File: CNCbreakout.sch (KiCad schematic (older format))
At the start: 18 parts, among them P101 X1, P102 X2, P103 Y, P104 Z, P105 GND, P106 +24V, P107 VFD_Stop, P108 VFD_FwdRev, P109 VFD_Aux, P110 Z_STOP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

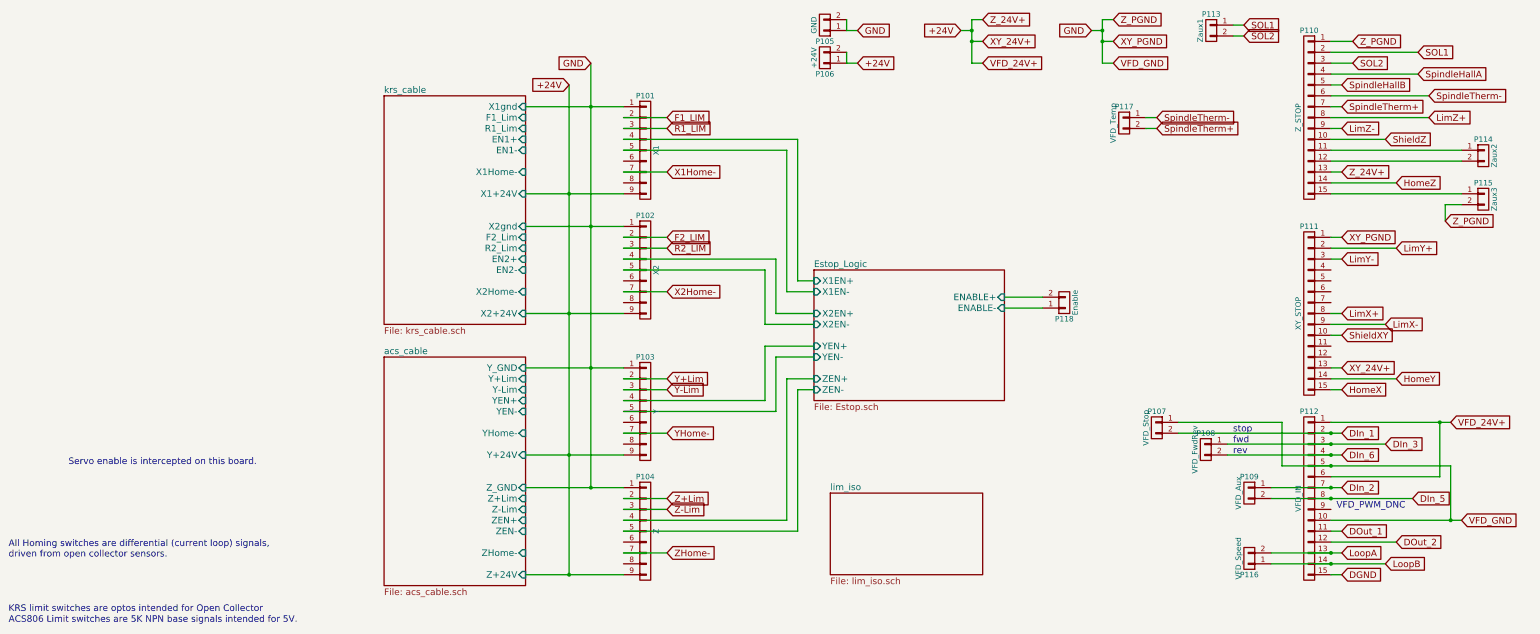
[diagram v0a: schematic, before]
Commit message: checked limits and homes, removed enable, adjusted routing
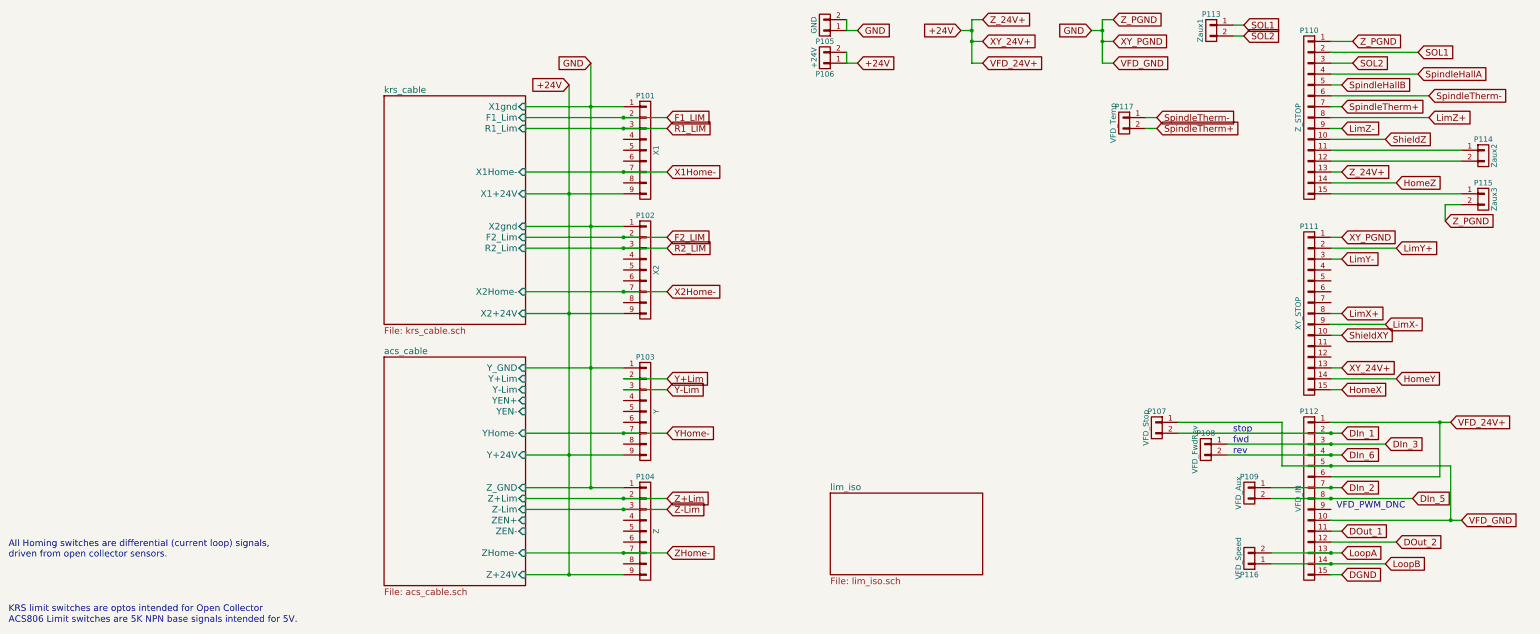
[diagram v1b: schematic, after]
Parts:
- removed P118: Enable, Connect:bornier2, symbol CONN_01X02
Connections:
- net Estop_Logic/X1EN+: no longer names the net of P101.4 (P4)
- net Estop_Logic/X1EN-: no longer names the net of P101.5 (P5)
- net Estop_Logic/X2EN+: no longer names the net of P102.4 (P4)
- net Estop_Logic/X2EN-: no longer names the net of P102.5 (P5)
- net Estop_Logic/YEN+: no longer names the net of P103.4 (P4)
- net Estop_Logic/YEN-: no longer names the net of P103.5 (P5)
- net Estop_Logic/ZEN+: no longer names the net of P104.4 (P4)
- net Estop_Logic/ZEN-: no longer names the net of P104.5 (P5)
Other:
- note removed: "Servo enable is intercepted on this board."
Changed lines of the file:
@@
 $Descr A4 11693 8268
 encoding utf-8
-Sheet 1 5
+Sheet 1 4
 Title ""
 Date ""
@@
 F3 "F1_Lim" I R 2100 1700 60
 F4 "R1_Lim" I R 2100 1800 60
-F5 "EN1+" I R 2100 1900 60
-F6 "EN1-" I R 2100 2000 60
-F7 "X1Home-" I R 2100 2200 60
-F8 "X1+24V" I R 2100 2400 60
-F9 "X2gnd" I R 2100 2700 60
-F10 "F2_Lim" I R 2100 2800 60
-F11 "R2_Lim" I R 2100 2900 60
-F12 "EN2+" I R 2100 3000 60
-F13 "EN2-" I R 2100 3100 60
-F14 "X2Home-" I R 2100 3300 60
-F15 "X2+24V" I R 2100 3500 60
+F5 "X1Home-" I R 2100 2200 60
+F6 "X1+24V" I R 2100 2400 60
+F7 "X2gnd" I R 2100 2700 60
+F8 "F2_Lim" I R 2100 2800 60
+F9 "R2_Lim" I R 2100 2900 60
+F10 "X2Home-" I R 2100 3300 60
+F11 "X2+24V" I R 2100 3500 60
 $EndSheet
-Text Notes -2100 4900 0    60   ~ 0
-Servo enable is intercepted on this board.
 Text GLabel 3400 2900 2    60   Input ~ 0
 R2_LIM
@@
 Text GLabel 7500 1200 2    60   Input ~ 0
 VFD_GND
-$Sheet
-S 4750 3100 1750 1200
-U 5792E5FC
-F0 "Estop_Logic" 60
-F1 "Estop.sch" 60
-F2 "ZEN+" I L 4750 4100 60
-F3 "ZEN-" I L 4750 4200 60
-F4 "YEN+" I L 4750 3800 60
-F5 "YEN-" I L 4750 3900 60
-F6 "X1EN+" I L 4750 3200 60
-F7 "X1EN-" I L 4750 3300 60
-F8 "X2EN+" I L 4750 3500 60
-F9 "X2EN-" I L 4750 3600 60
-F10 "ENABLE+" I R 6500 3350 60
-F11 "ENABLE-" I R 6500 3450 60
-$EndSheet
 Wire Wire Line
 	9700 1000 9500 1000
@@
 Connection ~ 7400 1000
 Wire Wire Line
-	3400 1700 3000 1700
-Wire Wire Line
-	3000 1800 3400 1800
-Wire Wire Line
-	3000 2200 3400 2200
-Wire Wire Line
-	3400 2800 3000 2800
-Wire Wire Line
-	3000 3300 3400 3300
-Wire Wire Line
-	3400 2900 3000 2900
+	2100 1700 3400 1700
+Wire Wire Line
+	2100 1800 3400 1800
+Wire Wire Line
+	2100 2200 3400 2200
+Wire Wire Line
+	2100 2800 3400 2800
+Wire Wire Line
+	2100 3300 3400 3300
+Wire Wire Line
+	2100 2900 3400 2900
 Wire Wire Line
 	3400 4100 3000 4100
@@
 	3000 4200 3400 4200
 Wire Wire Line
-	3000 4600 3400 4600
+	2100 4600 3400 4600
 Connection ~ 2700 5100
 Wire Wire Line
-	3000 5200 3400 5200
-Wire Wire Line
-	3400 5300 3000 5300
-Wire Wire Line
-	3400 5700 3000 5700
+	2100 5200 3400 5200
+Wire Wire Line
+	2100 5300 3400 5300
+Wire Wire Line
+	2100 5700 3400 5700
 Connection ~ 2500 5900
 $Comp
@@
 	-1   0    0    -1
 $EndComp
-Wire Wire Line
-	4750 3200 4600 3200
-Wire Wire Line
-	4600 3200 4600 1900
-Wire Wire Line
-	4600 1900 3000 1900
-Wire Wire Line
-	3000 2000 4500 2000
-Wire Wire Line
-	4500 2000 4500 3300
-Wire Wire Line
-	4500 3300 4750 3300
-Wire Wire Line
-	4750 3500 4400 3500
-Wire Wire Line
-	4400 3500 4400 3000
-Wire Wire Line
-	4400 3000 3000 3000
-Wire Wire Line
-	3000 3100 4300 3100
-Wire Wire Line
-	4300 3100 4300 3600
-Wire Wire Line
-	4300 3600 4750 3600
-Wire Wire Line
-	4750 3800 4300 3800
-Wire Wire Line
-	4300 3800 4300 4300
-Wire Wire Line
-	4300 4300 3000 4300
-Wire Wire Line
-	3000 4400 4400 4400
-Wire Wire Line
-	4400 4400 4400 3900
-Wire Wire Line
-	4400 3900 4750 3900
-Wire Wire Line
-	4750 4100 4500 4100
-Wire Wire Line
-	4500 4100 4500 5400
-Wire Wire Line
-	4500 5400 3000 5400
-Wire Wire Line
-	3000 5500 4600 5500
-Wire Wire Line
-	4600 5500 4600 4200
-Wire Wire Line
-	4600 4200 4750 4200
 $Comp
 L CONN_01X02 P113
@@
 Text GLabel 7900 1700 2    60   Input ~ 0
 SpindleTherm-
-$Comp
-L CONN_01X02 P118
-U 1 1 580D988B
-P 7050 3400
-F 0 "P118" H 7050 3550 50  0000 C CNN
-F 1 "Enable" V 7150 3400 50  0000 C CNN
-F 2 "Connect:bornier2" H 7050 3400 50  0001 C CNN
-F 3 "" H 7050 3400 50  0000 C CNN
-	1    7050 3400
-	1    0    0    1
-$EndComp
-Wire Wire Line
-	6500 3350 6850 3350
-Wire Wire Line
-	6850 3450 6500 3450
 $Sheet
 S 800  3900 1300 2100
@@
 F15 "Z+24V" I R 2100 5900 60
 $EndSheet
+Connection ~ 3000 2200
+Connection ~ 3000 3300
+Connection ~ 3000 4600
+Connection ~ 3000 5700
+Connection ~ 3000 5300
+Connection ~ 3000 5200
+Connection ~ 3000 1700
+Connection ~ 3000 1800
+Connection ~ 3000 2800
+Connection ~ 3000 2900
 $EndSCHEMATC
